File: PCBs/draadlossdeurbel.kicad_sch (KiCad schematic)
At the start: 16 parts, among them Q1 BC161, U1 WeMos_D1_mini, U2 LM386, U3 74HC595, U4 SN76489, U5 TP4056-breakout

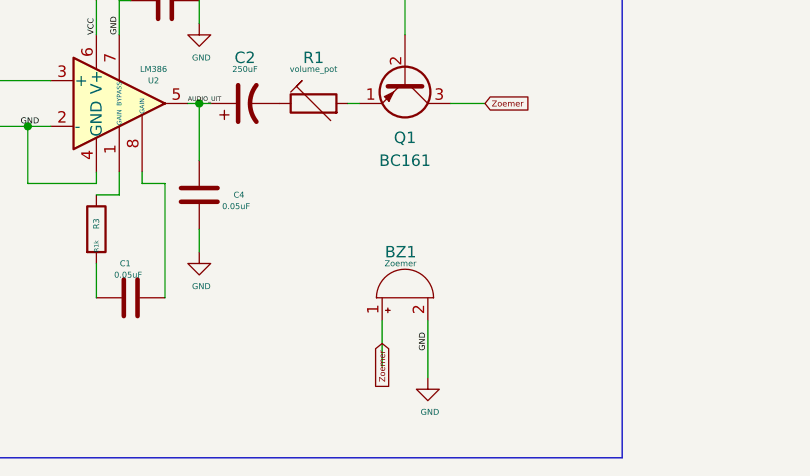
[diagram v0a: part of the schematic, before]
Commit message: 6581 SID biliotheek toegevoegd
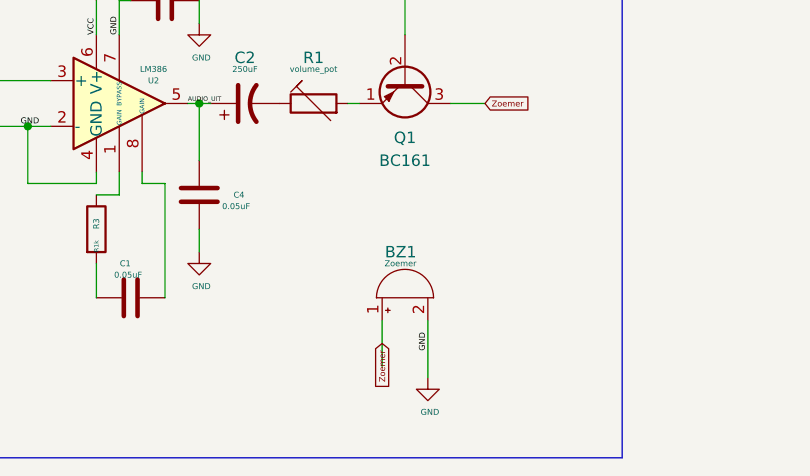
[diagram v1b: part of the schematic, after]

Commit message: Wireless Doorbell 0.0.2
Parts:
- removed D1: LED-R, symbol Device:LED
- removed U3: 74HC595, symbol 74xx:74HC595
- added J1: AudioPlug3, symbol Connector_Audio:AudioPlug3
- added R4, R5: R10k, symbol Device:R
- added U3: PCF8574, symbol Interface_Expansion:PCF8574
- R2: value R100 -> R10k
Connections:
- net LED is gone; now on net GND: R2.1
- net GND: now also R4.1, R5.1, U3.8 (VSS)
- net Qa: now also U3.4 (P0)
- net Qb: now also U3.5 (P1)
- net Qc: now also U3.6 (P2)
- net Qd: now also U3.7 (P3)
- net Qe: now also U3.9 (P4)
- net Qf: now also U3.10 (P5)
- net Qg: now also U3.11 (P6)
- net Qh: now also U3.12 (P7)
- net VCC: now also U3.16 (VDD)
- net A0: now reaches R2.2
- net A0: now also U3.1 (A0)
- new net: R5.2, U3.3 (A2)
- new net A1: R4.2, U3.2 (A1)
- no-connect marks 3 -> 4
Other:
- note added: "Wireless Doorbell 0.0.2 Work-in-progress!!"
- note removed: "Wireless Doorbell 0.0.1 Work-in-progress!!"
- moved on the sheet: U4

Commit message: Wireless Doorbell 0.0.2
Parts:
- added D1: LED, symbol Device:LED
- added J2, J3: I2C_Oled_128X32, symbol Connector_Generic:Conn_01x04
- added Q2: BC338, Package_TO_SOT_THT:TO-92_Inline, symbol Transistor_BJT:BC338
- added R6: R100, symbol Device:R
- added R7: R100, symbol Device:R_Small
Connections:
- net MOSI is gone; now on net WE: U1.6 (MOSI/D7)
- net SN76489_geluid is gone; now on net geluid: U2.3 (+), U4.7 (AUDIO_OUT)
- net GND: now also J1.S, J2.1 (Pin_1), J2.2 (Pin_2), J3.4 (Pin_4)
- net VCC: now also J2.3 (Pin_3), J3.3 (Pin_3)
- net WE: no longer U1.14 (SCL/D1)
- net Zoemer: now also R7.2
- net SCL: now reaches U3.14 (SCL)
- net SCL: now also U1.14 (SCL/D1), J3.2 (Pin_2)
- net SDA: now reaches U3.15 (SDA)
- net SDA: now also U1.13 (SDA/D2), J3.1 (Pin_1)
- net geluid: now reaches J1.R
- net geluid: now also J2.4 (Pin_4)
- net at J1.T: now also R6.2
- net AudioPlug3_AanUit: now reaches U1.12 (D3)
- net AudioPlug3_AanUit: now also Q2.2 (B)
- net Latch: no longer names the net of U1.7 (CS/D8)
- net SCK: no longer names the net of U1.5 (MISO/D6)
- new net: D1.1 (K), Q2.1 (C)
- new net: D1.2 (A), R7.1
- new net: Q2.3 (E), R6.1
- no-connect marks 4 -> 5
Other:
- note added: "Debug headers"

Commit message: Wireless Doorbell 0.0.2
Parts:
- removed BT1: Battery_Cell, symbol Device:Battery_Cell
- removed U5: TP4056-breakout, symbol EasyLab4Kids:TP4056-breakout
- added J4: TP4056_bat, Connector_PinSocket_1.27mm:PinSocket_1x04_P1.27mm_Vertical, symbol Connector_Generic:Conn_01x04
- BZ1: footprint (none) -> Buzzer_Beeper:Buzzer_12x9.5RM7.6
- C1: footprint (none) -> Capacitor_THT:C_Rect_L11.0mm_W8.8mm_P10.00mm_MKT
- C2, C3, C4: footprint (none) -> Capacitor_SMD:CP_Elec_8x6.2
- D1: footprint (none) -> LED_THT:LED_D3.0mm
- J2: value I2C_Oled_128X32 -> debug_01x04; footprint (none) -> Connector_PinSocket_1.27mm:PinSocket_1x04_P1.27mm_Vertical
- J3: footprint (none) -> Connector_PinSocket_1.27mm:PinSocket_1x04_P1.27mm_Vertical
- R1: footprint (none) -> Potentiometer_THT:Potentiometer_Vishay_43_Horizontal
- R2, R3, R4, R5, R6, R7: footprint (none) -> Resistor_THT:R_Axial_DIN0414_L11.9mm_D4.5mm_P7.62mm_Vertical
- U2: footprint (none) -> Package_DIP:DIP-8_W7.62mm
- U3: footprint (none) -> Package_DIP:DIP-16_W7.62mm
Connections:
- net GND: now also J4.1 (Pin_1)
- net VCC: now also J4.4 (Pin_4)
- new net bat_in+: J4.3 (Pin_3)
- no-connect marks 5 -> 7

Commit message: Wireless Doorbell 0.0.2
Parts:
- J1: footprint (none) -> Connector_Audio:Jack_3.5mm_CUI_SJ1-3535NG_Horizontal
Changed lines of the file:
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@@
+    (stroke (width 0) (type default))
+  )
+  (wire (pts (xy 177.8 44.831) (xy 180.34 44.831))
     (stroke (width 0) (type default))
   )
@@
   )
   (wire (pts (xy 71.12 124.46) (xy 72.39 124.46))
-    (stroke (width 0) (type default))
-  )
-  (wire (pts (xy 177.8 44.831) (xy 180.34 44.831))
     (stroke (width 0) (type default))
   )
@@
       (effects (font (size 1.27 1.27)) (justify right))
     )
-    (property "Footprint" "" (at 141.351 124.206 0)
-      (effects (font (size 1.27 1.27)) hide)
-    )
+    (property "Footprint" "Connector_Audio:Jack_3.5mm_CUI_SJ1-3535NG_Horizontal" (at 141.351 124.206 0)
+      (effects (font (size 1.27 1.27)) hide)
+    )

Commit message: Wireless Doorbell 0.0.2
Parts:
- removed R1: volume_pot, Potentiometer_THT:Potentiometer_Vishay_43_Horizontal, symbol Device:R_Trim
- added D2: Status_LED, LED_THT:LED_D3.0mm, symbol Device:LED
- added R8: R1k, Resistor_THT:R_Axial_DIN0414_L11.9mm_D4.5mm_P7.62mm_Vertical, symbol Device:R_Small
- added RV1: r_pot_vol, Rotary_Encoder:RotaryEncoder_Bourns_Horizontal_PEC09-2xxxF-Nxxxx, symbol Device:R_Potentiometer_Small
- C1: footprint Capacitor_THT:C_Rect_L11.0mm_W8.8mm_P10.00mm_MKT -> Capacitor_THT:CP_Radial_D4.0mm_P1.50mm
- C2, C3, C4: footprint Capacitor_SMD:CP_Elec_8x6.2 -> Capacitor_THT:CP_Radial_D4.0mm_P1.50mm
- Q1: value BC161 -> BC338; footprint Package_TO_SOT_THT:TO-39-3 -> Package_TO_SOT_THT:TO-92L_HandSolder
- U4: footprint w_pth_circuits:dil_16-300_socket -> Package_DIP:DIP-16_W7.62mm
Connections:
- net AUDIO_UIT: now also C2.2, RV1.1
- net GND: now also D2.1 (K)
- net VCC: now also RV1.2
- net bat_in-: now also J4.2 (Pin_2)
- net at Q1.1 (E): now also RV1.3
- net at U1.4 (SCK/D5): now also R8.1
- new net: D2.2 (A), R8.2
- no-connect marks 7 -> 9
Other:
- moved on the sheet: BZ1, C1, C2, C3, C4, Q1, R3, U2
